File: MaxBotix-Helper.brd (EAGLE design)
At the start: 19.7 x 14.2 mm, 4 parts

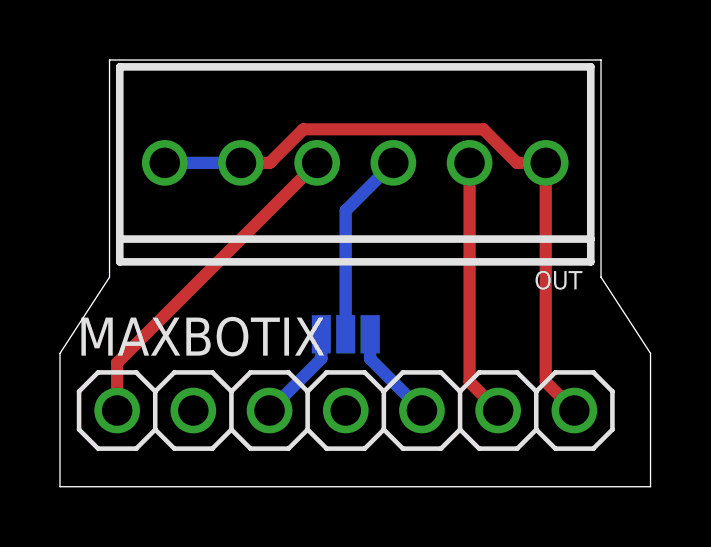
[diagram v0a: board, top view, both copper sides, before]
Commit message: Silk screen cleanup
Cleaned up/reorganized the silkscreen
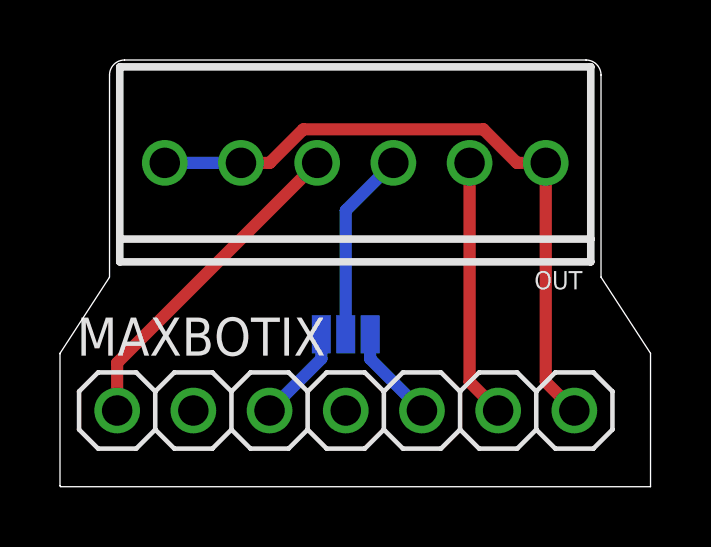
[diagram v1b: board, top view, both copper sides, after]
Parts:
- moved LOGO1 14.0 mm to (16.5, 5.21), flipped to the bottom
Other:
- outline, holes or cut-outs redrawn
- board text added: "AV"
- board text removed: "VA"
